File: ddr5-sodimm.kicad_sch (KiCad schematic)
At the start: 35 parts, among them J10 SSW-103-03-F-S, J2 Bus_DDR5_SODIMM_Amphenol_1016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, Q10 BSS138PW,115, Q11 BSS138PW,115, Q9 BSS138PW,115, SW3 SW_KMR211NGLFS_SMD, U35 INA293A5IDBVR

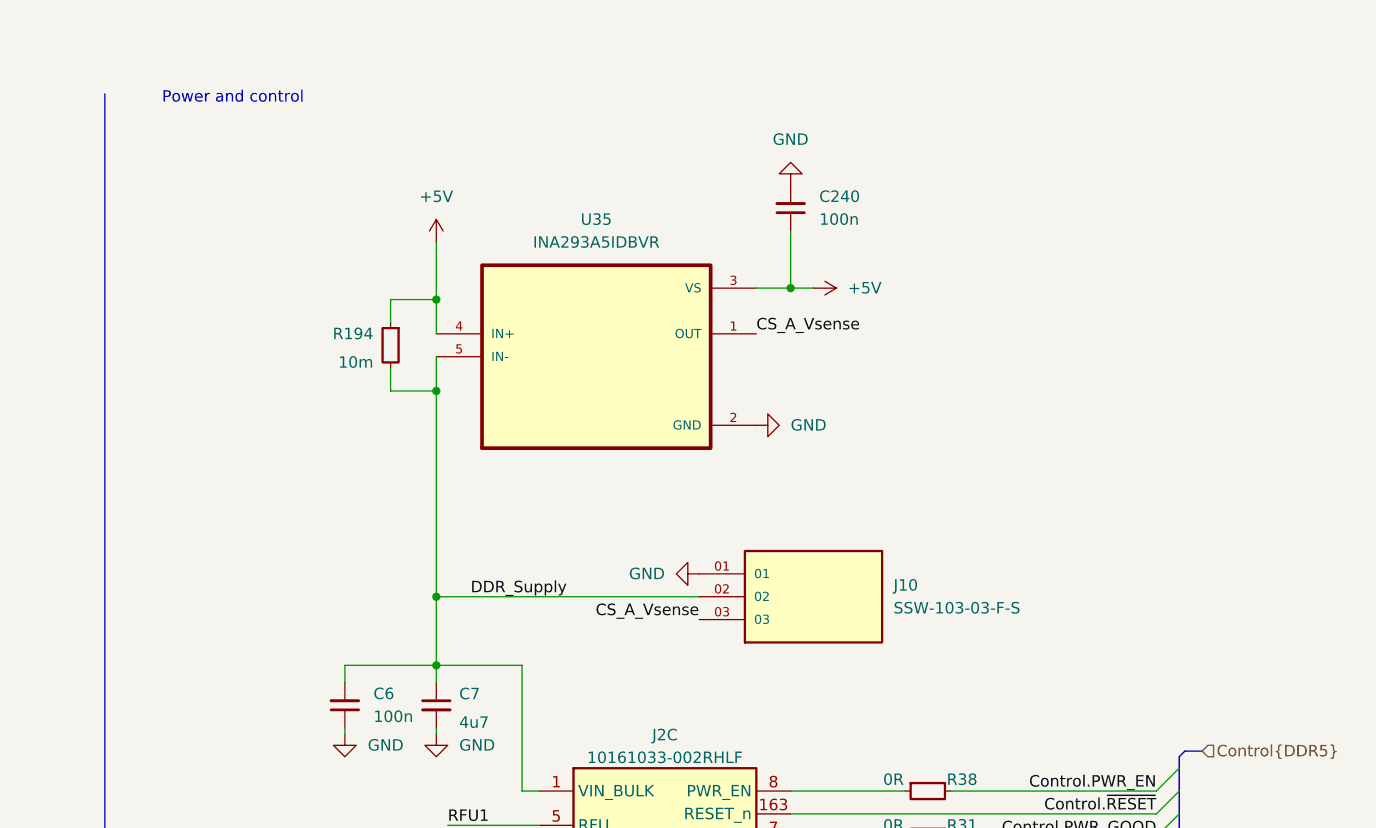
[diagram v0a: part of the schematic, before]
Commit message: Modified Sense Resistor to Kelvin Style
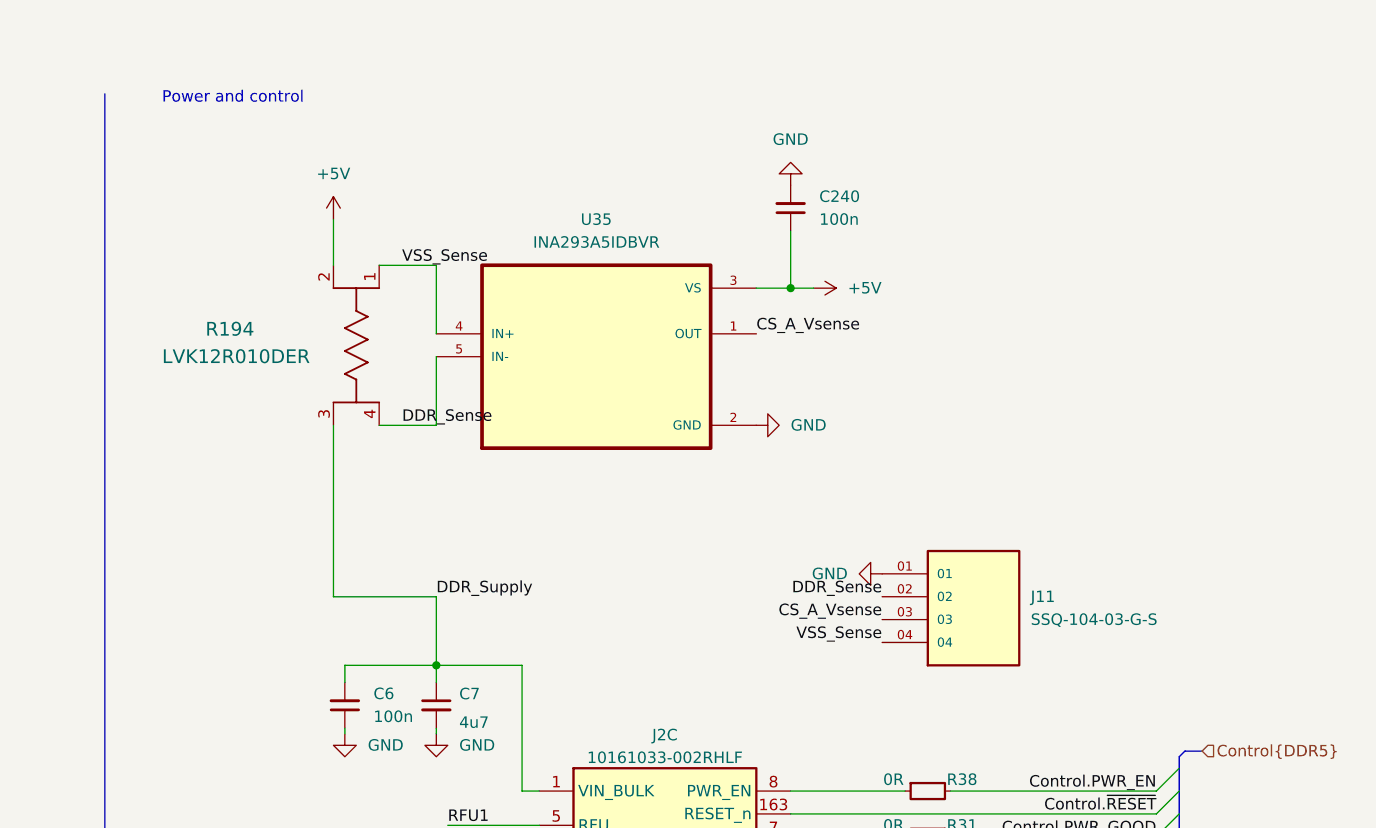
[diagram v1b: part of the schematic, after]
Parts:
- removed J10: SSW-103-03-F-S, Footprints:SAMTEC_SSW-103-03-F-S, symbol Symbols:SSW-103-03-F-S
- removed R194: R_10m_0402, Resistor_SMD:R_0402_1005Metric, symbol antmicroResistors0402:R_4k7_0402
- added J11: SSQ-104-03-G-S, Footprints:SAMTEC_SSQ-104-03-G-S, symbol Symbols:SSQ-104-03-G-S
- added R194: LVK12R010DER, Footprints:OH_LVK12_OHM, symbol Symbols:LVK12R010DER
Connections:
- net +5V: now also R194.2; no longer U35.4 (IN+)
- net CS_A_Vsense: now also J11.03
- net DDR_Supply: now also R194.3; no longer U35.5 (IN-)
- net GND: now also J11.01
- new net DDR_Sense: J11.02, R194.4, U35.5 (IN-)
- new net VSS_Sense: J11.04, R194.1, U35.4 (IN+)

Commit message: Should be ready
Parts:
- C240: footprint Capacitor_SMD:C_0402_1005Metric -> antmicro-footprints:C_0402_1005Metric
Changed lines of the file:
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@@
 			)
 		)
-		(property "Footprint" "Capacitor_SMD:C_0402_1005Metric"
+		(property "Footprint" "antmicro-footprints:C_0402_1005Metric"
 			(at 330.2 20.32 0)
 			(hide yes)
